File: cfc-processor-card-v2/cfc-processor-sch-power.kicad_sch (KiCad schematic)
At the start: 91 parts, among them Q1 DMP2240UDM, Q2 PMV45EN, Q3 DMP3050LVT-7, Q4 DMP3050LVT-7, Q5 PMV45EN, U1 MAX7310ATE+, U2 MIC842LYC5, U3 MIC842LYC5, U4 TS5A21366, U5 MAX4211FETE, U6 TPS62112

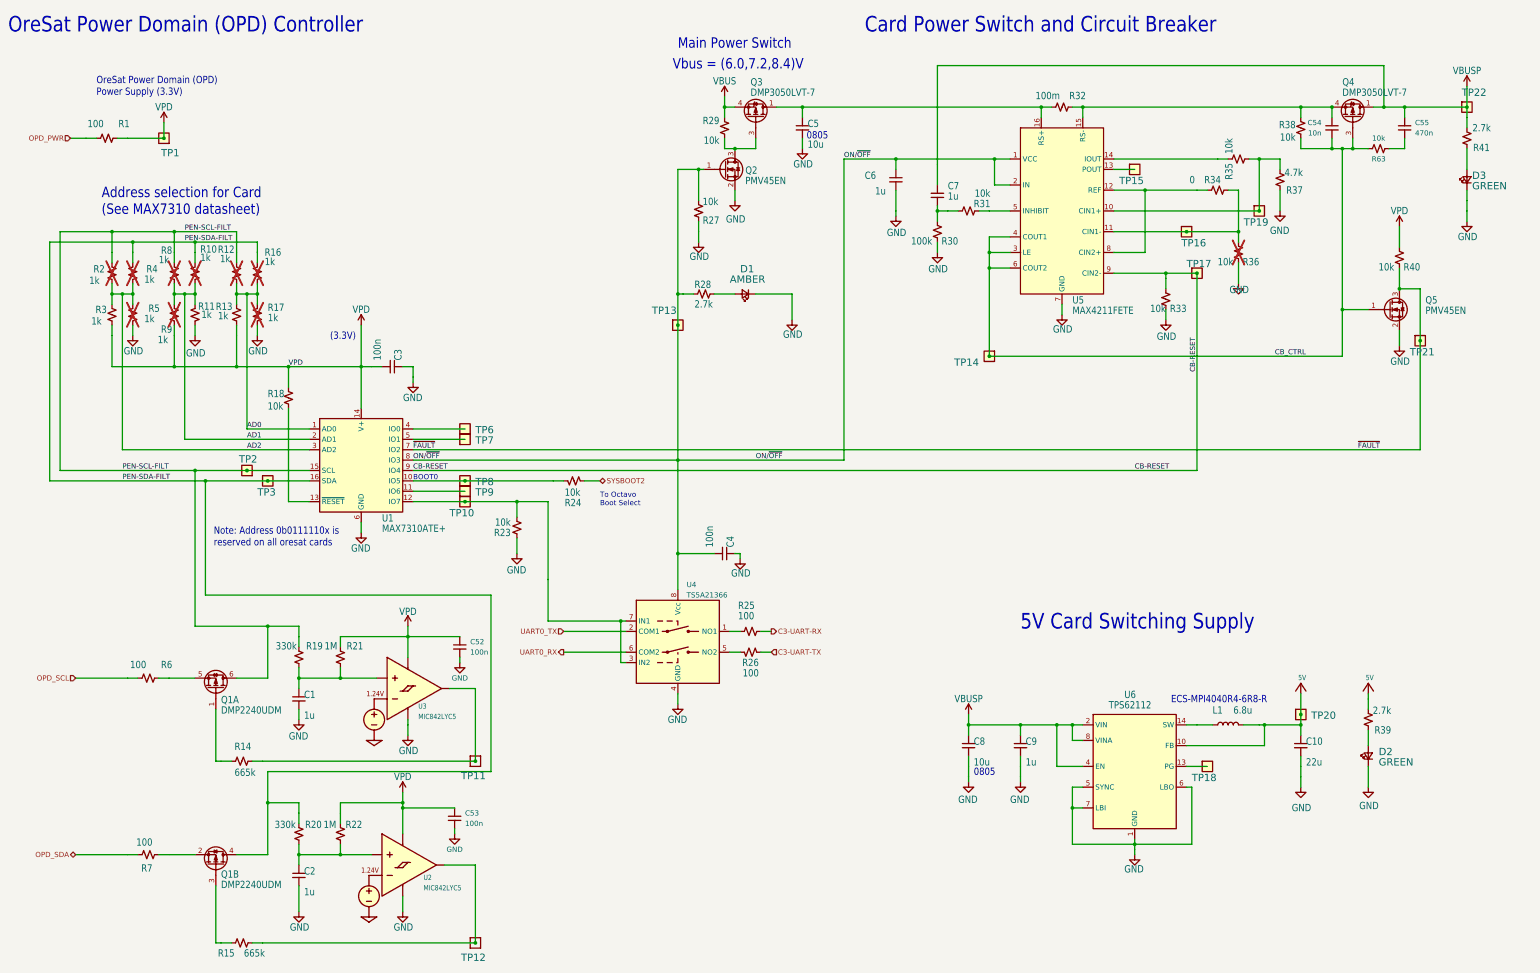
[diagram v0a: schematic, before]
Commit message: Update
updated opd address resistors to 100 ohms from 100 ohms, changed the 100 ohm res VBUSP to 10 ohms. Updated TEC page for sensor to have bidirectional current sense for diag. Removed misc testpoints
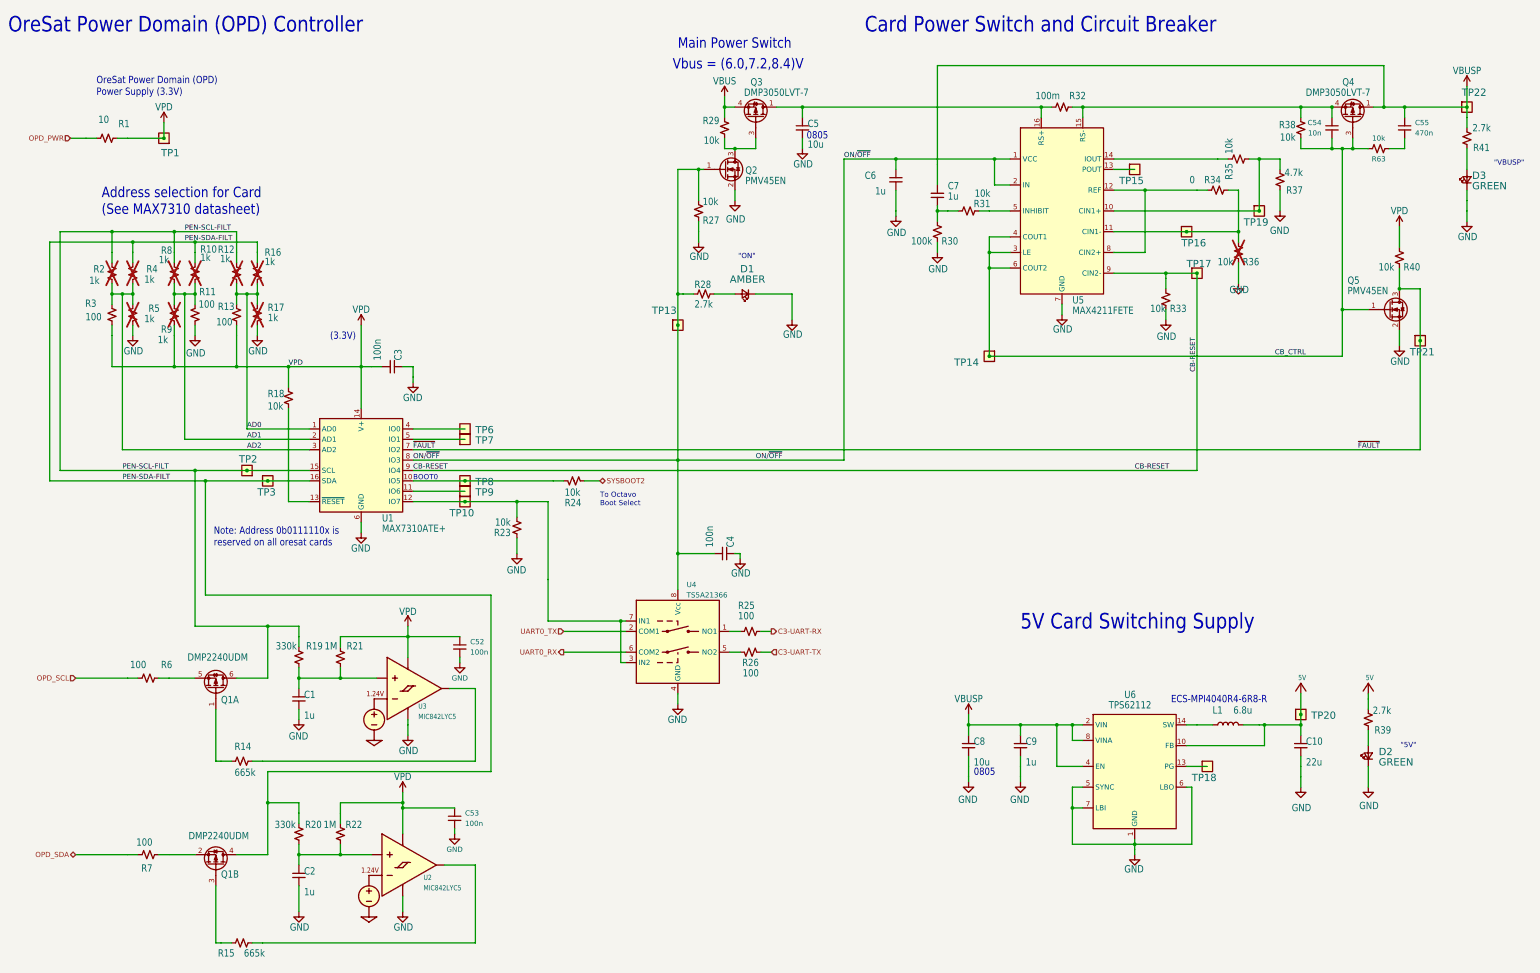
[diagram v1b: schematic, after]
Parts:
- removed TP11, TP12: TEST-POINT, cfc-card:2MM-TEST-POINT, symbol cfc-card-eagle-import:TEST-POINT
- Q2, Q5: footprint Package_TO_SOT_SMD:SOT-23-3 -> Package_TO_SOT_SMD:SOT-23
- R1: value 100 -> 10; DPN RMCF0603FT100RCT-ND -> RMCF0603FT10R0CT-ND; MPN RMCF0603FT100R -> RMCF0603FT10R0
- R11, R13, R3: value 1k -> 100; DPN RMCF0603FT1K00CT-ND -> RMCF0603FT100RCT-ND; MPN RMCF0603FT1K00 -> RMCF0603FT100R
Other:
- note added: ""5V""
- note added: ""ON""
- note added: ""VBUSP""
